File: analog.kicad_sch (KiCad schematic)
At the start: 51 parts, among them J10 Sensor harness, U8 ADS1115

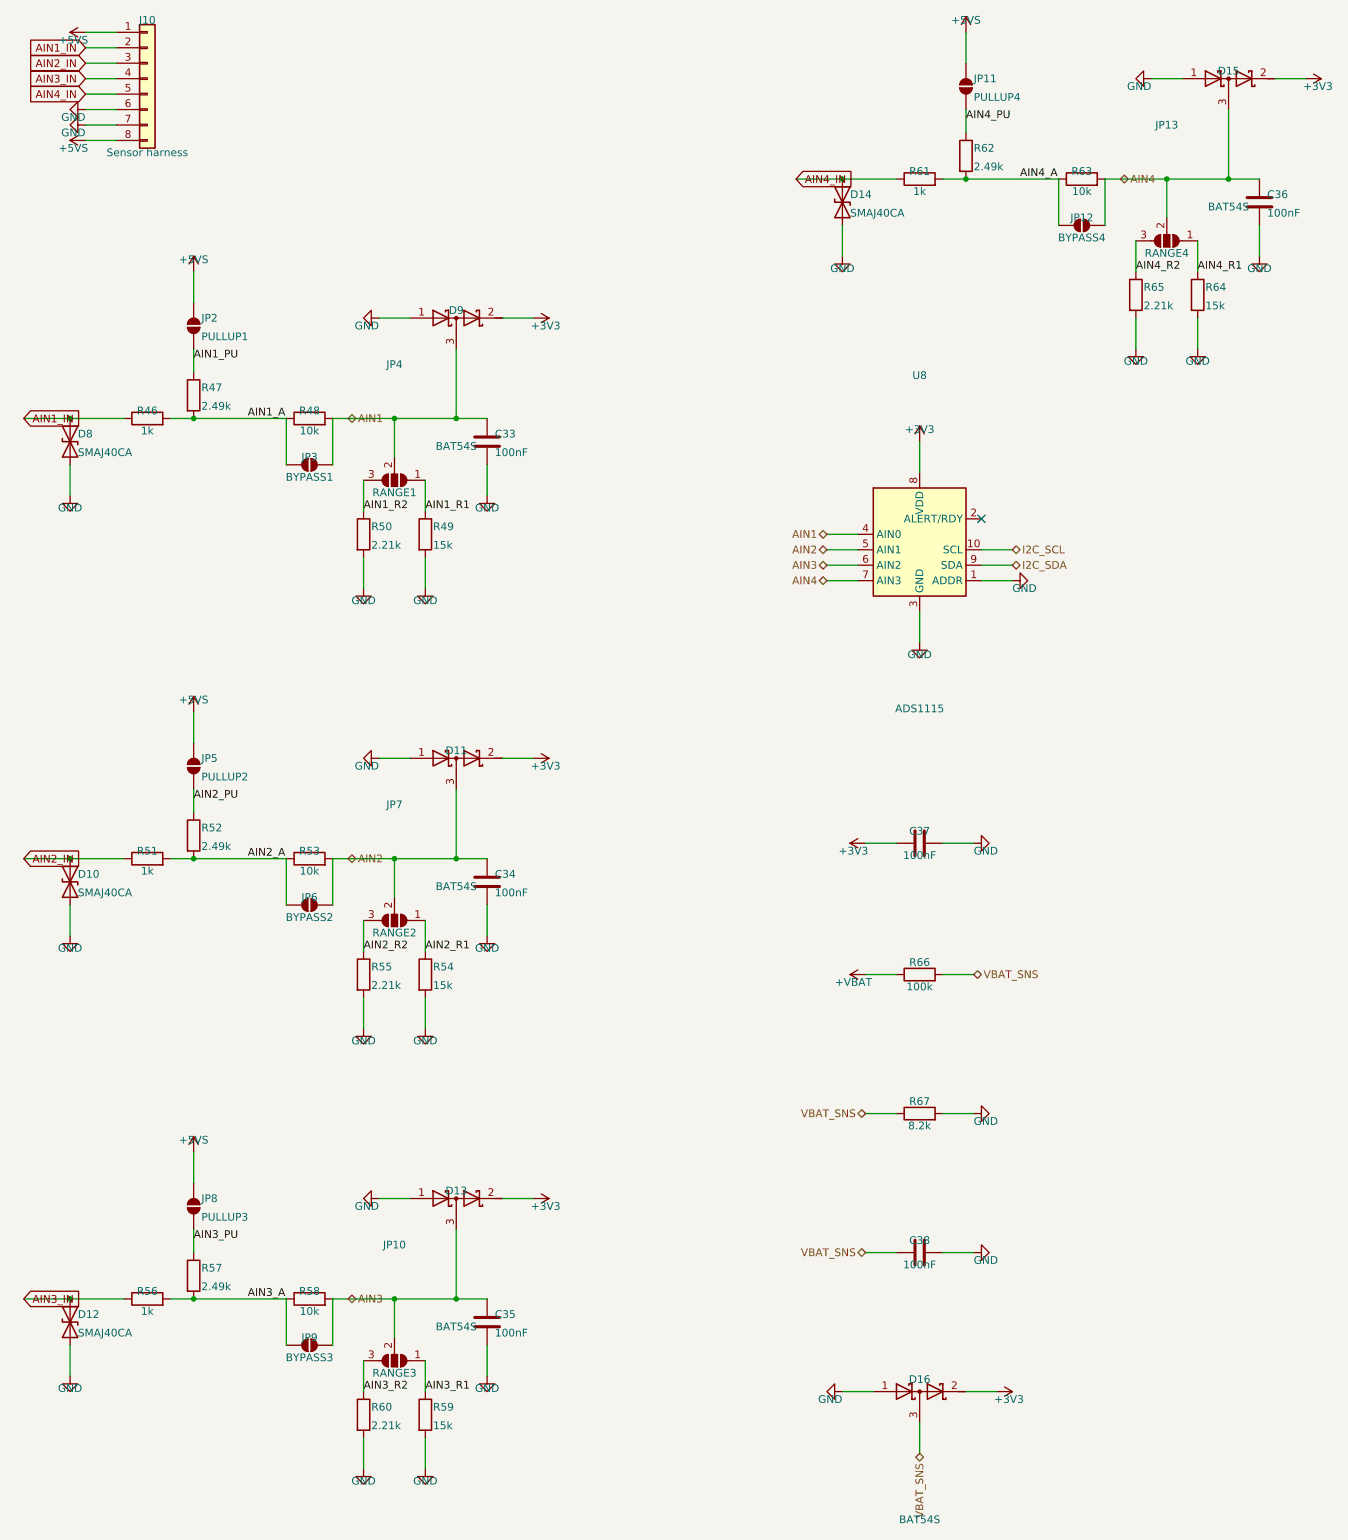
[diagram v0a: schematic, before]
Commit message: Power-fail ride-through: detect, coast, shed; board grows to 84 x 100
The ignition cuts this board's power with a log file open, every drive.
Three new pieces make that survivable, all simulated before layout:

- Detect: TLV431 + 100k/12.7k divider on VBAT_F, AHEAD of the ideal
  diode, asserting PWR_FAIL (IO15) at 11.0 V with ~0.3 V hysteresis.
  The harness collapses microseconds after the key turns while +VBAT
  coasts, so the warning costs no stored energy.
- Coast: two 220 uF/100 V cans join the 100 uF on +VBAT. 540 uF on the
  input rail, where a volt of headroom is worth most.
- Shed: AO3401 + 2N7002 high-side switch on the sensor rail (SENS_EN,
  IO16, off at reset), with PF1 moved behind it so a tripped sensor
  fuse can also be power-cycled from firmware.

Simulated end to end: detection <1 ms after the cut, then 108 ms to
converter dropout with sensors shed, 53 ms without -- the switch doubles
the flush budget. ISO pulse 1's brownout shortens from 8.2 to 5.6 ms.

The two cans plus the detector had no free board left on 84 x 84, so the
board grows to 84 x 100 (still JLC's cheap tier): bottom-edge furniture
and mounting holes move down 16 mm, one can per side, and the detector/
switch column gets its own placement zone. Also included from the audit:
the 3V3 buck's own input capacitor pair at its VIN pin (it was reaching
12.6 mm across to the 5 V island's), the CAN transceiver and AHCT buffer
bypasses pinned at their pins, and Power-class tracks at 0.55 mm to clear
IPC-2221 for 2 A at a 20 C rise.

Hard-won generator fix: a literal newline inside a symbol property is
accepted by KiCad's loader but silently breaks connectivity for every
symbol after it in the file -- the netlist dropped 45 components with no
error pointing anywhere near the cause. The emitter now flattens all
whitespace in property strings.

Board: 0 DRC violations, 0 unconnected, physical audit clean end to end.
185 components, 111 nets, ERC clean, netlist verified node-for-node.

Co-Authore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
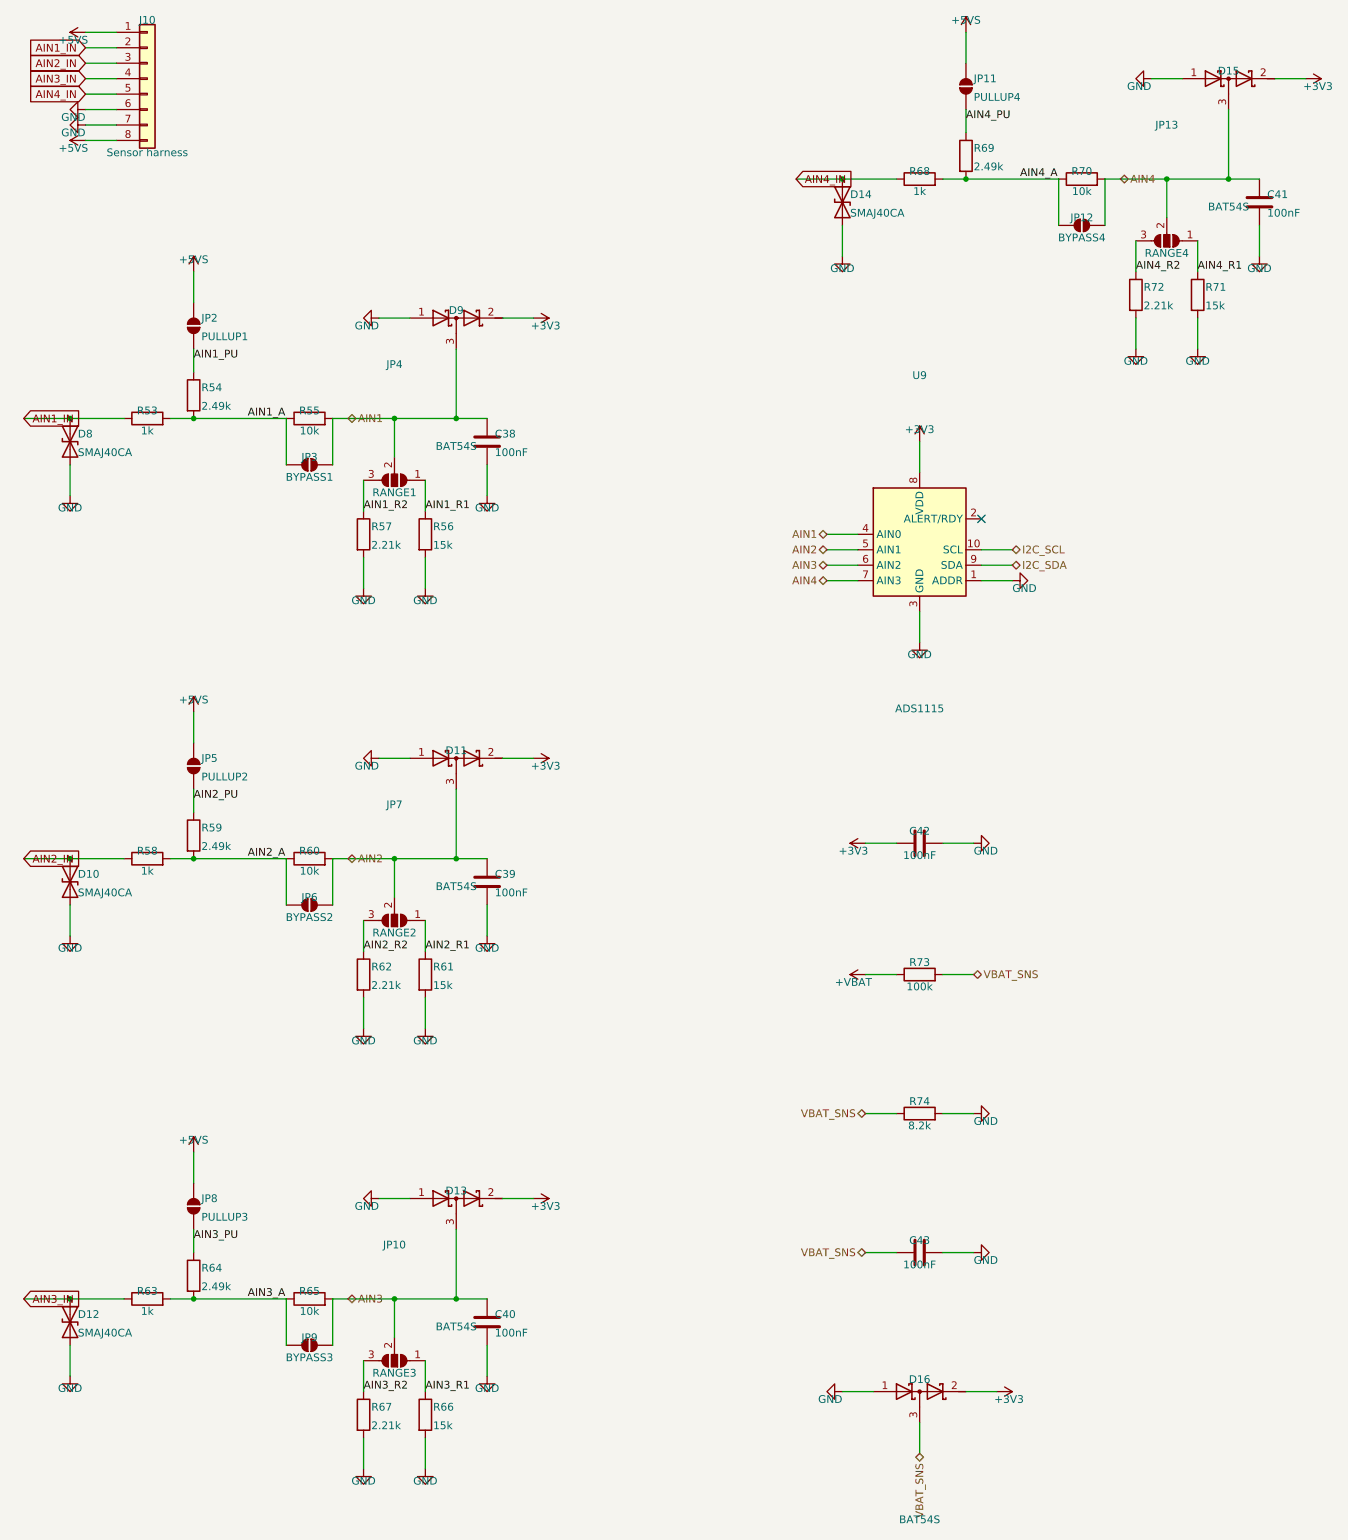
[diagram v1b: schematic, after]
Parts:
- removed C33, C34, C35, C36, C37: 100nF, Capacitor_SMD:C_0805_2012Metric, symbol Device:C
- removed R46, R51: 1k, Resistor_SMD:R_0805_2012Metric, symbol Device:R
- removed R47, R52: 2.49k, Resistor_SMD:R_0805_2012Metric, symbol Device:R
- removed R48: 10k, Resistor_SMD:R_0805_2012Metric, symbol Device:R
- removed R49: 15k, Resistor_SMD:R_0805_2012Metric, symbol Device:R
- removed R50: 2.21k, Resistor_SMD:R_0805_2012Metric, symbol Device:R
- removed U8: ADS1115, Package_SO:VSSOP-10_3x3mm_P0.5mm, symbol Analog_ADC:ADS1115IDGS
- added C39, C40, C41, C42, C43: 100nF, Capacitor_SMD:C_0805_2012Metric, symbol Device:C
- added R68: 1k, Resistor_SMD:R_0805_2012Metric, symbol Device:R
- added R69: 2.49k, Resistor_SMD:R_0805_2012Metric, symbol Device:R
- added R70: 10k, Resistor_SMD:R_0805_2012Metric, symbol Device:R
- added R71: 15k, Resistor_SMD:R_0805_2012Metric, symbol Device:R
- added R72: 2.21k, Resistor_SMD:R_0805_2012Metric, symbol Device:R
- added R73: 100k, Resistor_SMD:R_0805_2012Metric, symbol Device:R
- added R74: 8.2k, Resistor_SMD:R_0805_2012Metric, symbol Device:R
- added U9: ADS1115, Package_SO:VSSOP-10_3x3mm_P0.5mm, symbol Analog_ADC:ADS1115IDGS
- C38: Note (none) -> Ch1 anti-alias / ADC charge reservoir
- R53: value 10k -> 1k; Note Ch2 divider upper leg, 0.1% thin film for AFR-grade accuracy -> Ch1 series/fault-current limit; 0.1% thin film -- it is ins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
- R54: value 15k -> 2.49k; Note 0-5V range: 5.0V in -> ~2.88V at the ADC (1k series include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 -> Ch1 bias resistor; Tolerance 0.1% -> (none)
- R55: value 2.21k -> 10k; Note 0-16V range: 16.0V in -> ~2.67V at the ADC (1k series inclu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 -> Ch1 divider upper leg, 0.1% thin film for AFR-grade accuracy
- R56: value 1k -> 15k; Note Ch3 series/fault-current limit; 0.1% thin film -- it is ins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 -> 0-5V range: 5.0V in -> ~2.88V at the ADC (1k series include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
- R57: value 2.49k -> 2.21k; Note Ch3 bias resistor -> 0-16V range: 16.0V in -> ~2.67V at the ADC (1k series inclu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; Tolerance (none) -> 0.1%
- R58: value 10k -> 1k; Note Ch3 divider upper leg, 0.1% thin film for AFR-grade accuracy -> Ch2 series/fault-current limit; 0.1% thin film -- it is ins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
- R59: value 15k -> 2.49k; Note 0-5V range: 5.0V in -> ~2.88V at the ADC (1k series include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 -> Ch2 bias resistor; Tolerance 0.1% -> (none)
- R60: value 2.21k -> 10k; Note 0-16V range: 16.0V in -> ~2.67V at the ADC (1k series inclu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 -> Ch2 divider upper leg, 0.1% thin film for AFR-grade accuracy
- R61: value 1k -> 15k; Note Ch4 series/fault-current limit; 0.1% thin film -- it is ins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 -> 0-5V range: 5.0V in -> ~2.88V at the ADC (1k series include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
- R62: value 2.49k -> 2.21k; Note Ch4 bias resistor -> 0-16V range: 16.0V in -> ~2.67V at the ADC (1k series inclu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; Tolerance (none) -> 0.1%
- R63: value 10k -> 1k; Note Ch4 divider upper leg, 0.1% thin film for AFR-grade accuracy -> Ch3 series/fault-current limit; 0.1% thin film -- it is ins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
- R64: value 15k -> 2.49k; Note 0-5V range: 5.0V in -> ~2.88V at the ADC (1k series include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 -> Ch3 bias resistor; Tolerance 0.1% -> (none)
- R65: value 2.21k -> 10k; Note 0-16V range: 16.0V in -> ~2.67V at the ADC (1k series inclu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 -> Ch3 divider upper leg, 0.1% thin film for AFR-grade accuracy
- R66: value 100k -> 15k; Note Battery monitor: divide by 11 -> 0-5V range: 5.0V in -> ~2.88V at the ADC (1k series include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; Tolerance (none) -> 0.1%
- R67: value 8.2k -> 2.21k; Note Divide by 13.2, not 11: at 36V the 11:1 divider put 3.27V o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 -> 0-16V range: 16.0V in -> ~2.67V at the ADC (1k series inclu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; Tolerance (none) -> 0.1%
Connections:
- net +3V3: now also C42.1, U9.8 (VDD)
- net +VBAT: now also R73.1; no longer R66.1
- net AIN1: now also C38.1, R55.2, U9.4 (AIN0)
- net AIN1_A: now also R53.2, R54.2, R55.1
- net AIN1_IN: now also R53.1
- net AIN1_PU: now also R54.1
- net AIN1_R1: now also R56.1
- net AIN1_R2: now also R57.1
- net AIN2: now also R60.2, C39.1, U9.5 (AIN1); no longer R53.2
- net AIN2_A: now also R58.2, R59.2, R60.1; no longer R53.1
- net AIN2_IN: now also R58.1
- net AIN2_PU: now also R59.1
- net AIN2_R1: now also R61.1; no longer R54.1
- net AIN2_R2: now also R62.1; no longer R55.1
- net AIN3: now also R65.2, C40.1, U9.6 (AIN2); no longer R58.2
- net AIN3_A: now also R63.2, R64.2, R65.1; no longer R56.2, R57.2, R58.1
- net AIN3_IN: now also R63.1; no longer R56.1
- net AIN3_PU: now also R64.1; no longer R57.1
- net AIN3_R1: now also R66.1; no longer R59.1
- net AIN3_R2: now also R67.1; no longer R60.1
- net AIN4: now also C41.1, R70.2, U9.7 (AIN3); no longer R63.2
- net AIN4_A: now also R68.2, R69.2, R70.1; no longer R61.2, R62.2, R63.1
- net AIN4_IN: now also R68.1; no longer R61.1
- net AIN4_PU: now also R69.1; no longer R62.1
- net AIN4_R1: now also R71.1; no longer R64.1
- net AIN4_R2: now also R72.1; no longer R65.1
- net GND: now also R56.2, R57.2, R61.2, R62.2, R66.2, C39.2, C40.2, C41.2, C42.2, C43.2, R71.2, R72.2, R74.2, U9.1 (ADDR), U9.3 (GND); no longer R54.2, R55.2, R59.2, R60.2, R64.2, R65.2
- net I2C_SCL: now also U9.10 (SCL)
- net I2C_SDA: now also U9.9 (SDA)
- net VBAT_SNS: now also C43.1, R73.2, R74.1; no longer C38.1, R66.2, R67.1
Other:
- moved on the sheet: C38, R53, R54, R55, R56, R57, R58, R59, R60, R61, R62, R63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
